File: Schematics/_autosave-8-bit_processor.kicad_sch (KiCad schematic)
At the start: 34 parts, among them Q10 NPN, Q11 NPN, Q12 NPN, Q13 NPN, Q14 NPN, Q15 NPN, Q16 NPN, Q17 NPN, Q18 NPN, Q19 NPN, Q20 NPN, Q21 NPN, Q3 NPN, Q4 NPN, Q5 NPN, Q6 NPN, Q7 NPN, Q8 NPN, Q9 NPN

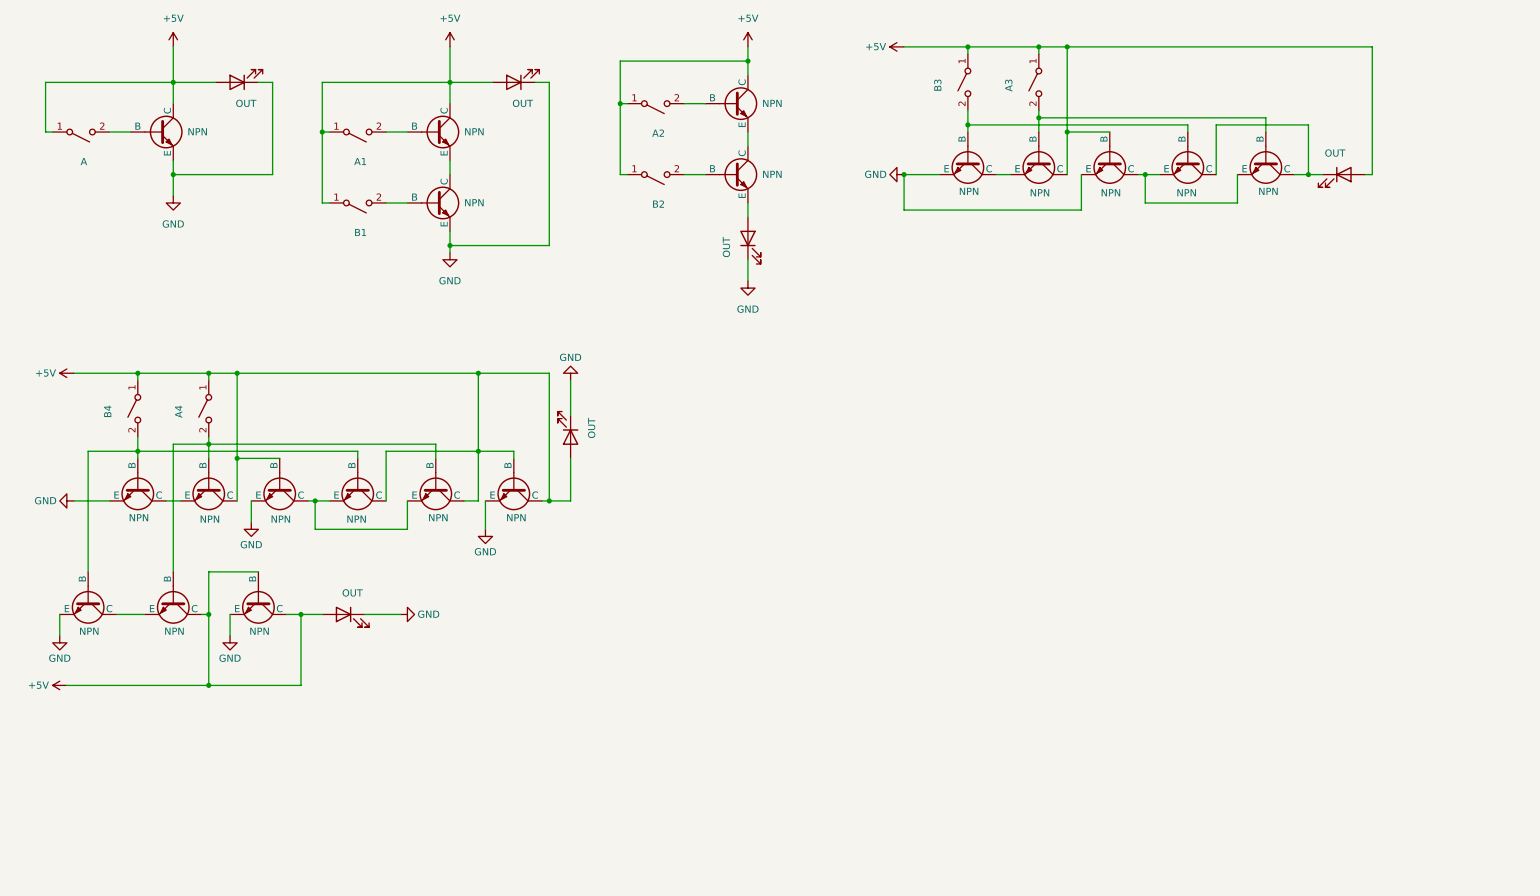
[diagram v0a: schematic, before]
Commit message: Added full adder images and schematics
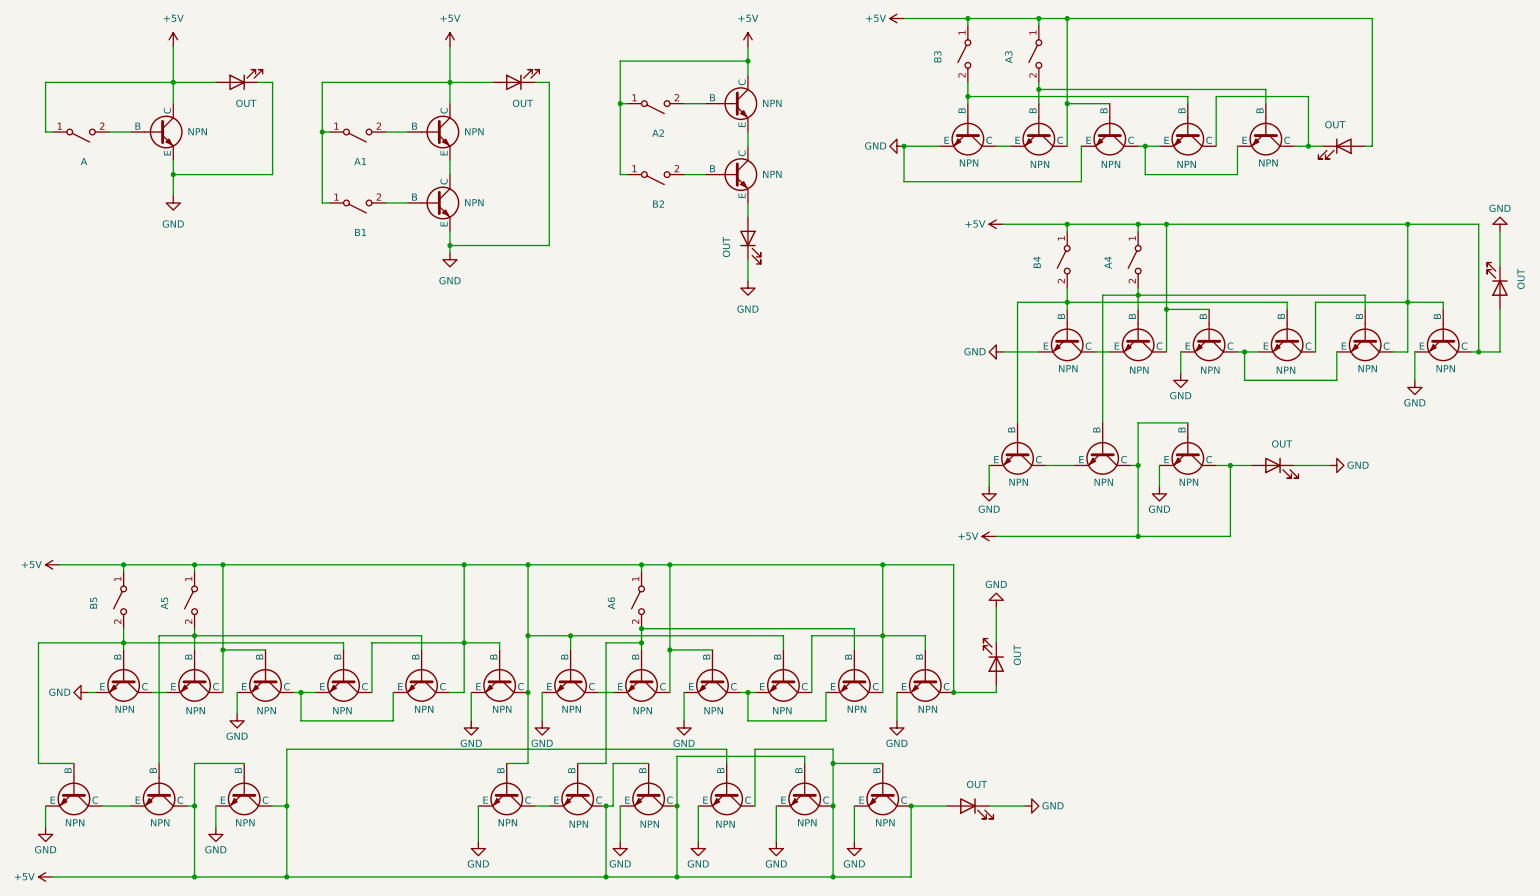
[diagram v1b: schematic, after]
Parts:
- added A5, A6, B5: SW_SPST, symbol Switch:SW_SPST
- added D7, D8: OUT, symbol Device:LED
- added Q22, Q23, Q24, Q25, Q26, Q27, Q28, Q29, Q30, Q31, Q32, Q33, Q34, Q35, Q36, Q37, Q38, Q39, Q40, Q41, Q42: NPN, symbol Simulation_SPICE:NPN
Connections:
- net +5V: now also A5.1 (A), A6.1 (A), B5.1 (A), D7.2 (A), D8.2 (A), Q24.1 (C), Q25.1 (C), Q26.1 (C), Q26.2 (B), Q27.2 (B), Q28.1 (C), Q29.1 (C), Q30.1 (C), Q30.2 (B), Q31.2 (B), Q32.1 (C), Q33.2 (B), Q34.1 (C), Q34.2 (B), Q35.1 (C), Q36.1 (C), Q36.2 (B), Q37.2 (B), Q38.1 (C), Q39.1 (C), Q39.2 (B), Q40.1 (C), Q40.2 (B), Q41.1 (C), Q41.2 (B), Q42.1 (C), Q42.2 (B)
- net GND: now also D7.1 (K), D8.1 (K), Q22.3 (E), Q23.3 (E), Q26.3 (E), Q27.3 (E), Q30.3 (E), Q31.3 (E), Q33.3 (E), Q36.3 (E), Q37.3 (E), Q39.3 (E), Q40.3 (E), Q41.3 (E), Q42.3 (E)
- new net: A5.2 (B), Q24.2 (B), Q25.2 (B), Q29.2 (B)
- new net: Q22.1 (C), Q24.3 (E)
- new net: Q27.1 (C), Q28.3 (E), Q29.3 (E)
- new net: B5.2 (B), Q22.2 (B), Q23.2 (B), Q28.2 (B)
- new net: A6.2 (B), Q32.2 (B), Q35.2 (B), Q38.2 (B)
- new net: Q33.1 (C), Q34.3 (E), Q35.3 (E)
- new net: Q23.1 (C), Q25.3 (E)
- new net: Q37.1 (C), Q38.3 (E)
- new net: Q31.1 (C), Q32.3 (E)
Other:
- moved on the sheet: A3, A4, B3, B4
